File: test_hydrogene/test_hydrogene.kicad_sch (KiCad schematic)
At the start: 7 parts, among them U3 STM32G474RBTx

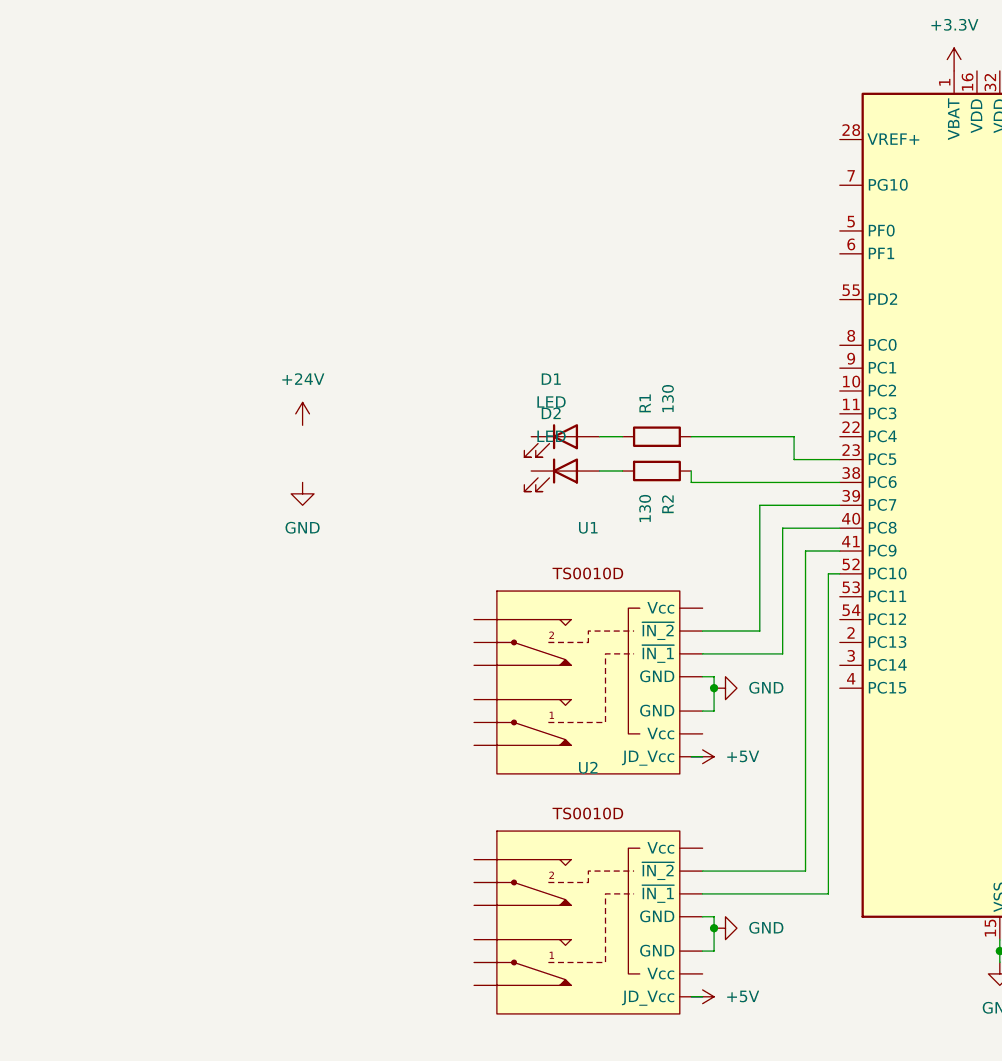
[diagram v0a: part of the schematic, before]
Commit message: Ajout des actuateurs
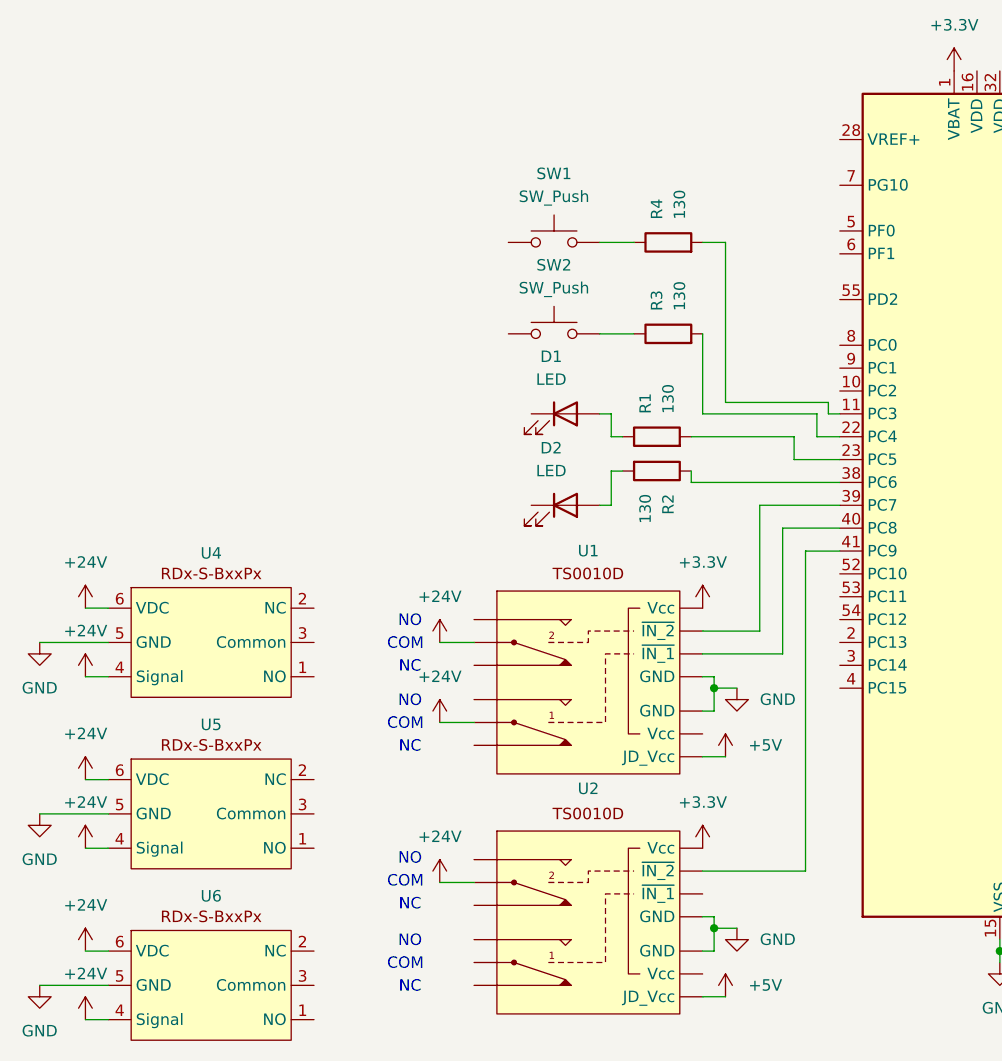
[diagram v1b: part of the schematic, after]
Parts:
- added R3, R4: 130, symbol Device:R
- added SW1, SW2: SW_Push, symbol Switch:SW_Push
- added U4, U5, U6: ~, symbol Actuator:RDx-S-BxxPx
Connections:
- net +24V: now also U1. (JD_Vcc), U2. (JD_Vcc), U4.4 (Signal), U4.6 (VDC), U5.4 (Signal), U5.6 (VDC), U6.4 (Signal), U6.6 (VDC)
- net +3.3V: now also U1. (JD_Vcc), U2. (JD_Vcc)
- net GND: now also U4.5 (GND), U5.5 (GND), U6.5 (GND)
- net at U3.11 (PC3): now also R4.2
- net at U3.22 (PC4): now also R3.2
- net at U3.52 (PC10): no longer U2. (JD_Vcc)
- new net: R4.1, SW1.2
- new net: R3.1, SW2.2
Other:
- note added: "COM"
- note added: "NC"
- note added: "NO"
- moved on the sheet: D1, D2

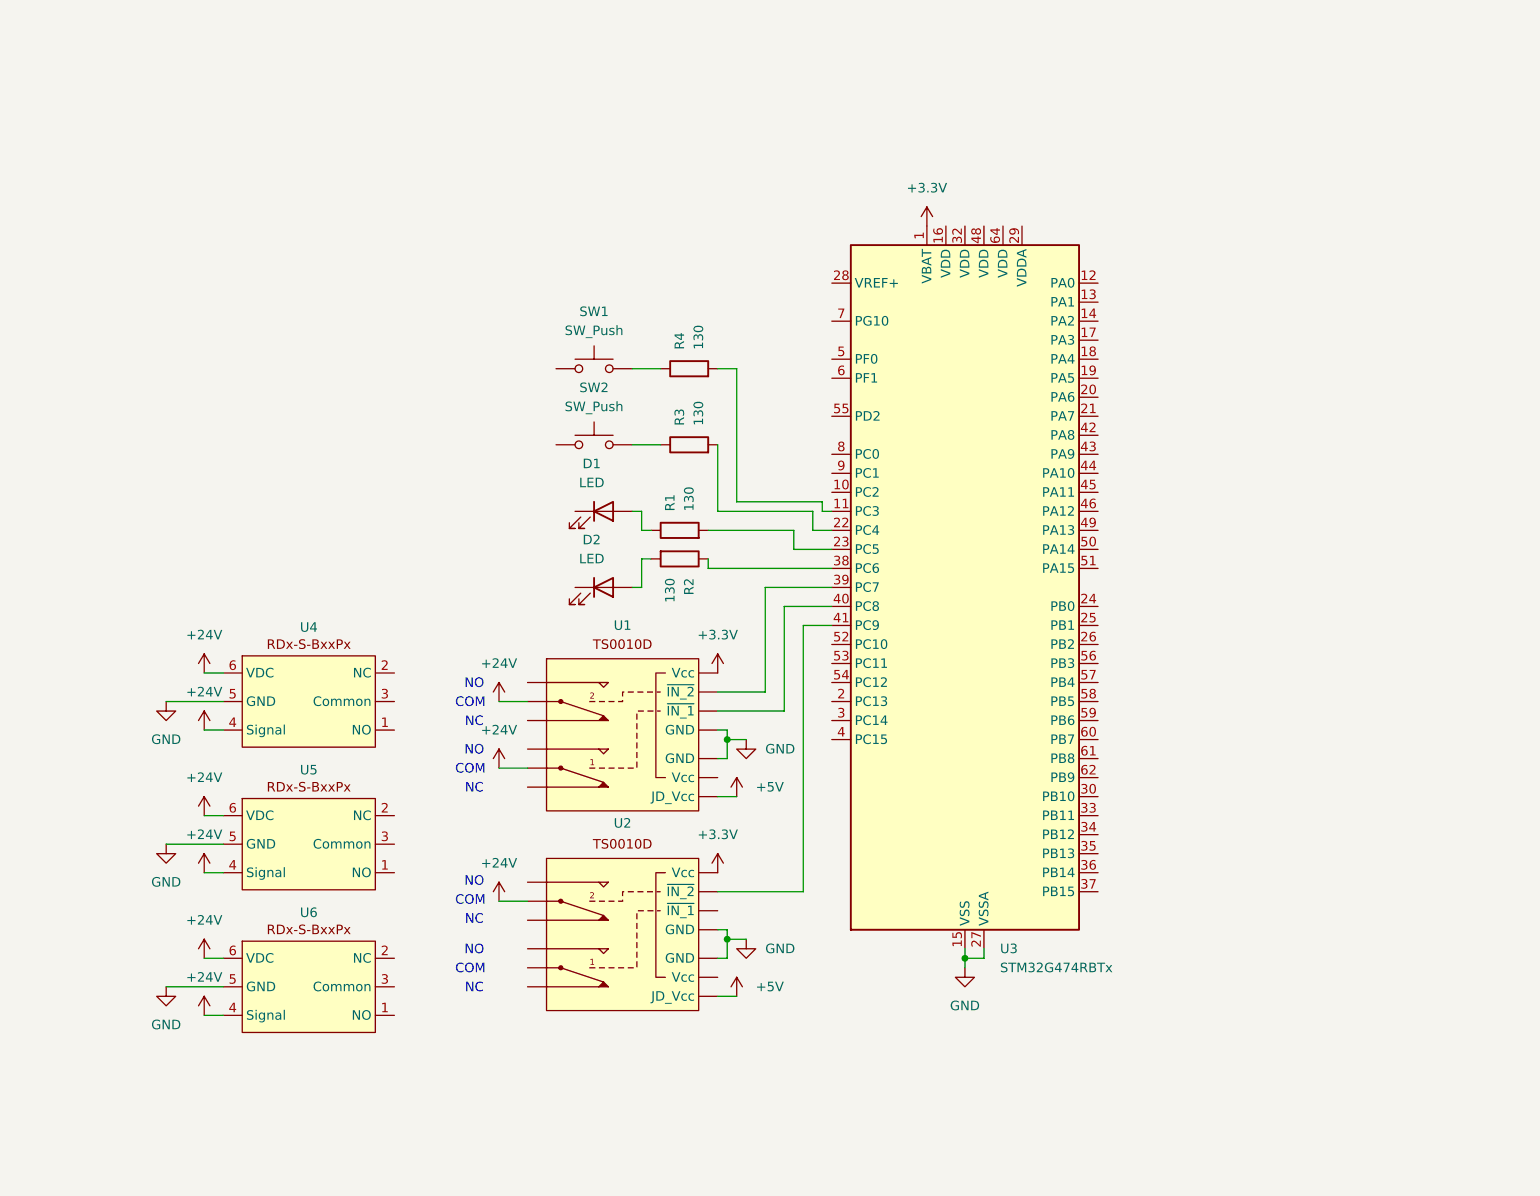
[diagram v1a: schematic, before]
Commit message: Connection des actuateurs
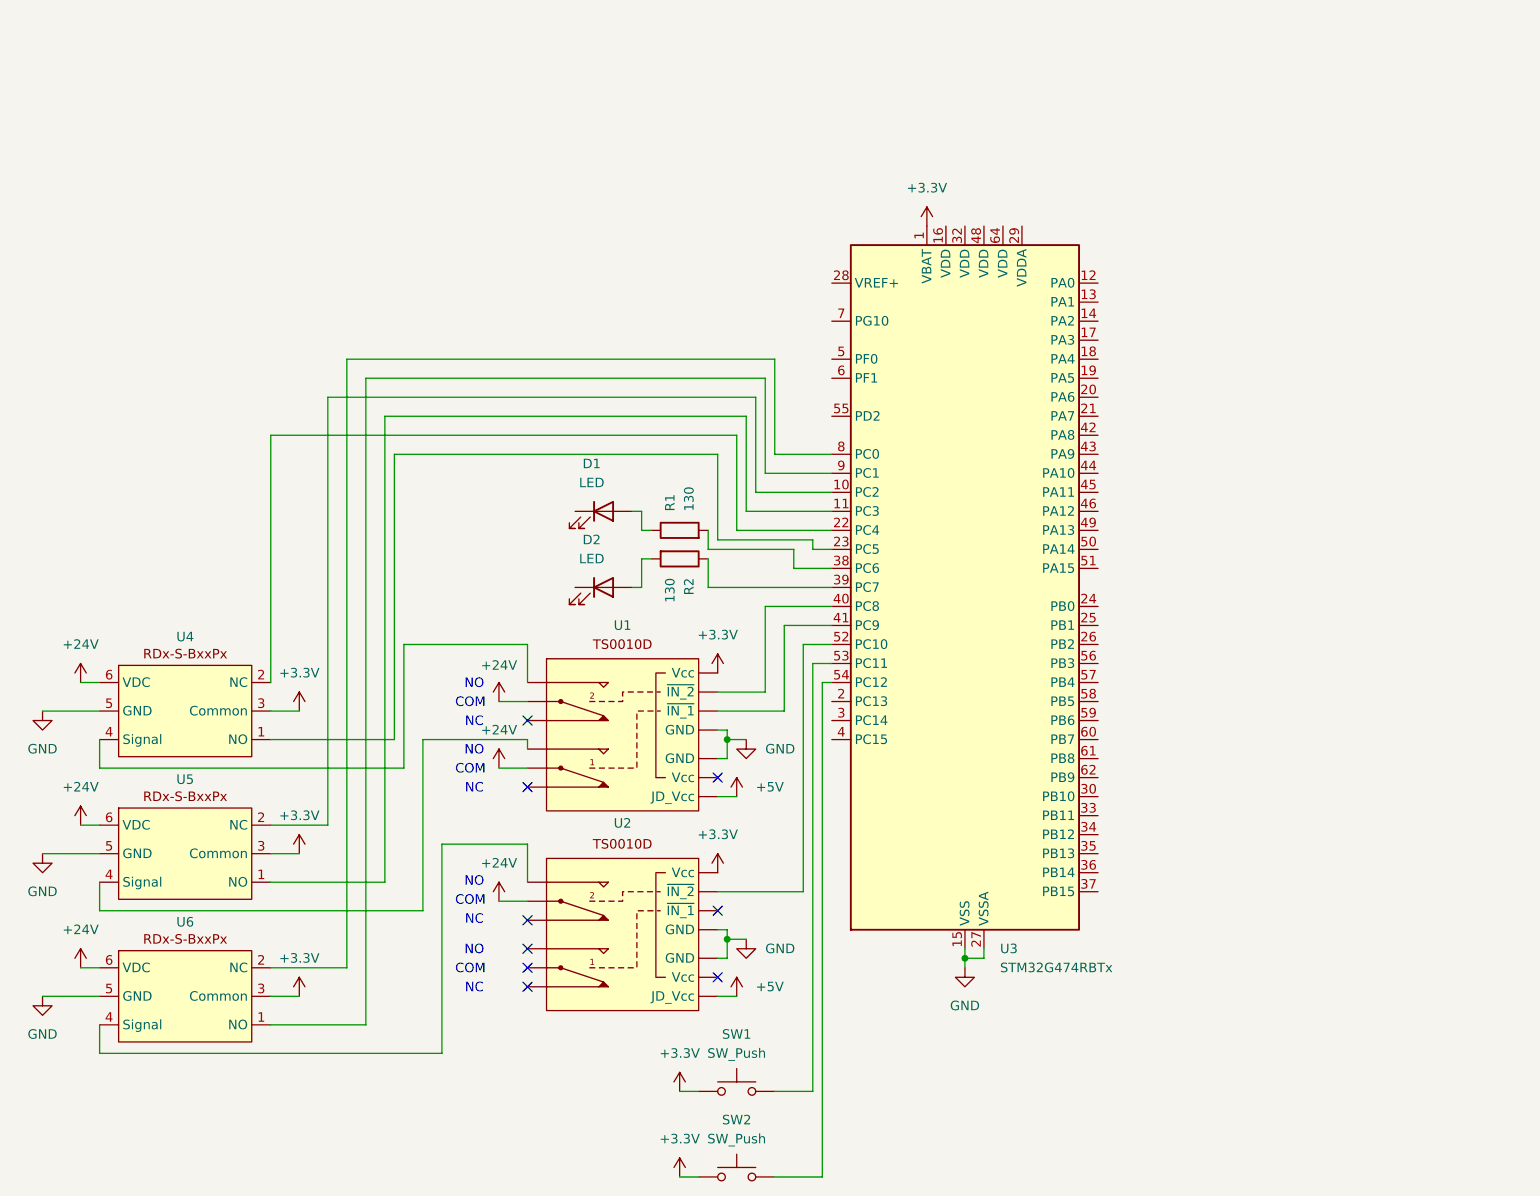
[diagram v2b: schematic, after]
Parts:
- removed R3, R4: 130, symbol Device:R
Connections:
- net +24V: no longer U4.4 (Signal), U5.4 (Signal), U6.4 (Signal)
- net +3.3V: now also SW1.1, SW2.1, U4.3 (Common), U5.3 (Common), U6.3 (Common)
- net at U5.1 (NO): now also U3.11 (PC3)
- net at U5.2 (NC): now also U3.10 (PC2)
- net at SW1.2: now also U3.53 (PC11)
- net at U3.39 (PC7): now also R2.1; no longer U1. (JD_Vcc)
- net at SW2.2: now also U3.54 (PC12)
- net at U6.1 (NO): now also U3.9 (PC1)
- net at U6.2 (NC): now also U3.8 (PC0)
- net at U3.22 (PC4): now also U4.2 (NC)
- net at U3.23 (PC5): now also U4.1 (NO); no longer R1.2
- net at U3.38 (PC6): now also R1.2; no longer R2.1
- net at U3.41 (PC9): now also U1. (JD_Vcc); no longer U2. (JD_Vcc)
- net at U3.52 (PC10): now also U2. (JD_Vcc)
- new net: U1. (JD_Vcc), U5.4 (Signal)
- new net: U1. (JD_Vcc), U4.4 (Signal)
- new net: U2. (JD_Vcc), U6.4 (Signal)
- no-connect marks 0 -> 9
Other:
- moved on the sheet: SW1, SW2, U4, U5, U6

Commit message: Simplifié le schéma
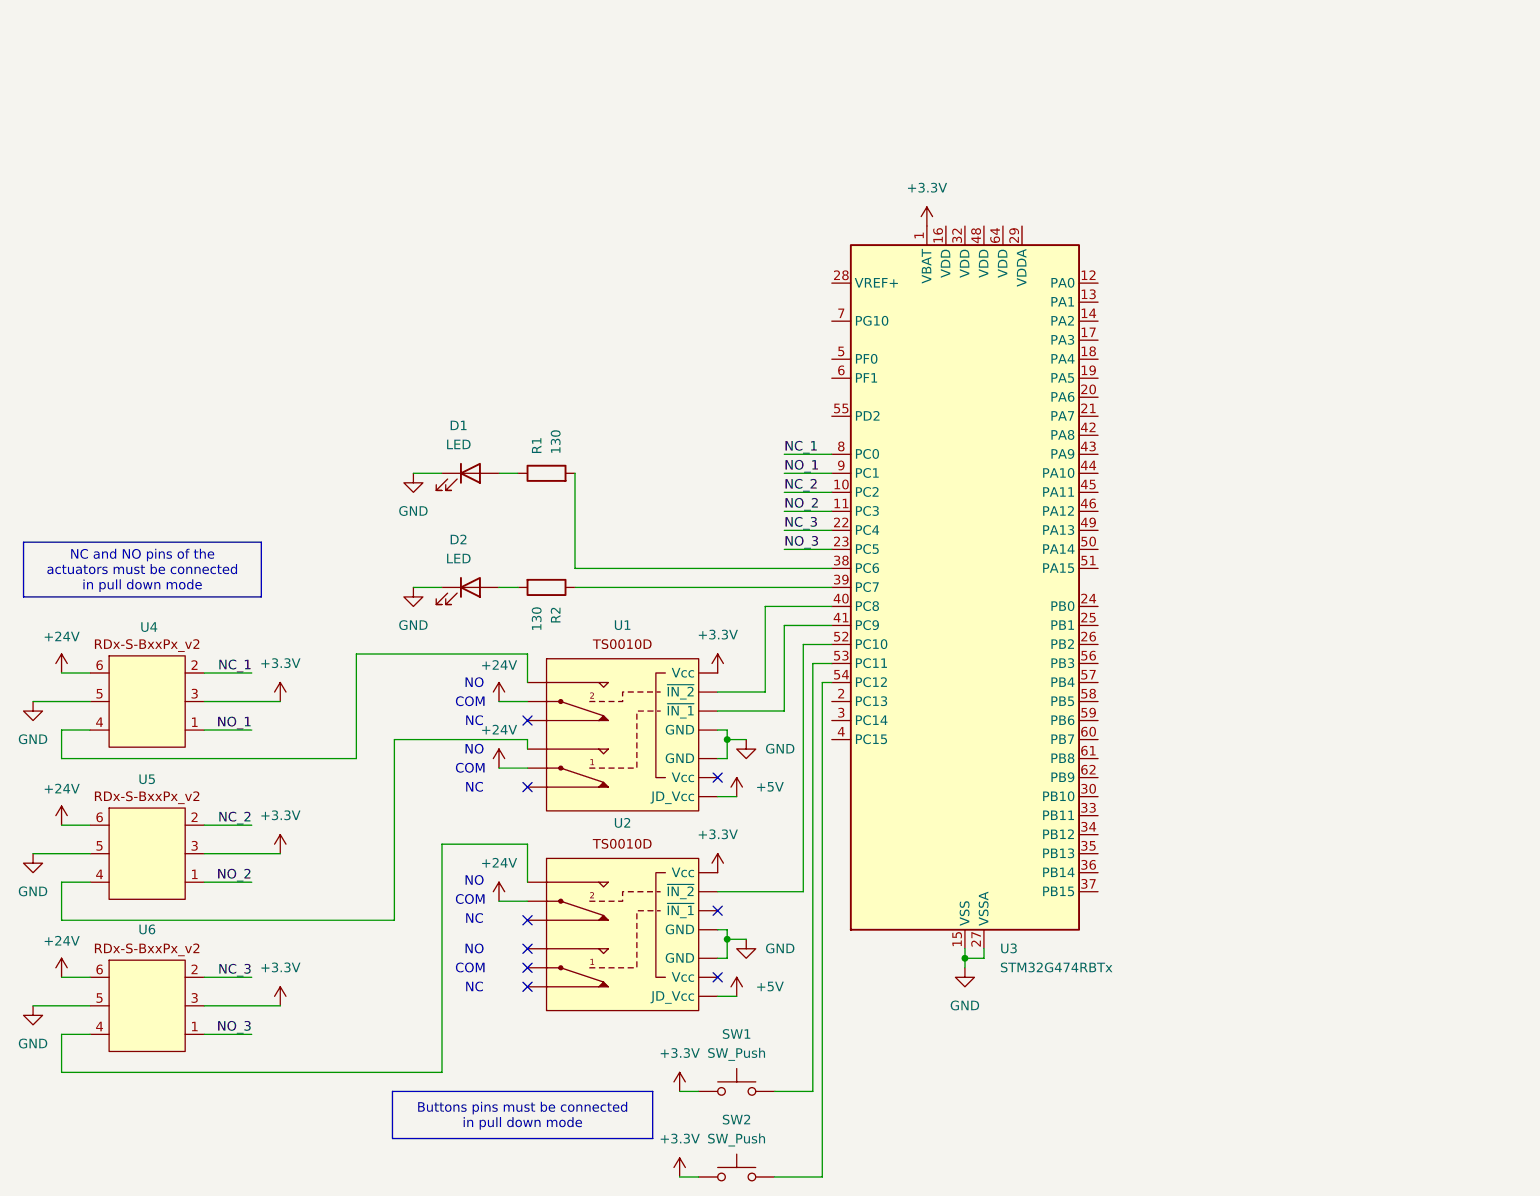
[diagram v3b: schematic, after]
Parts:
- removed U4, U5, U6: ~, symbol Actuator:RDx-S-BxxPx
- added U4, U5, U6: ~, symbol Actuator:RDx-S-BxxPx_v2
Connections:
- net +24V: now also U4.6, U5.6, U6.6
- net +3.3V: now also U4.3, U5.3, U6.3
- net GND: now also D1.1 (K), D2.1 (K), U4.5, U5.5, U6.5
- net NO_2: now reaches U3.11 (PC3)
- net NO_2: now also U5.1
- net NC_2: now reaches U3.10 (PC2)
- net NC_2: now also U5.2
- net NO_1: now reaches U3.9 (PC1)
- net NO_1: now also U4.1
- net NC_1: now reaches U3.8 (PC0)
- net NC_1: now also U4.2
- net NC_3: now reaches U3.22 (PC4)
- net NC_3: now also U6.2
- net NO_3: now reaches U3.23 (PC5)
- net NO_3: now also U6.1
- new net: U1. (JD_Vcc), U4.4
- new net: U1. (JD_Vcc), U5.4
- new net: U2. (JD_Vcc), U6.4
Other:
- company: (none) -> Exocet Polytechnique Montréal
- title: (none) -> Test Hydrogène
- moved on the sheet: D1, D2, R1, R2

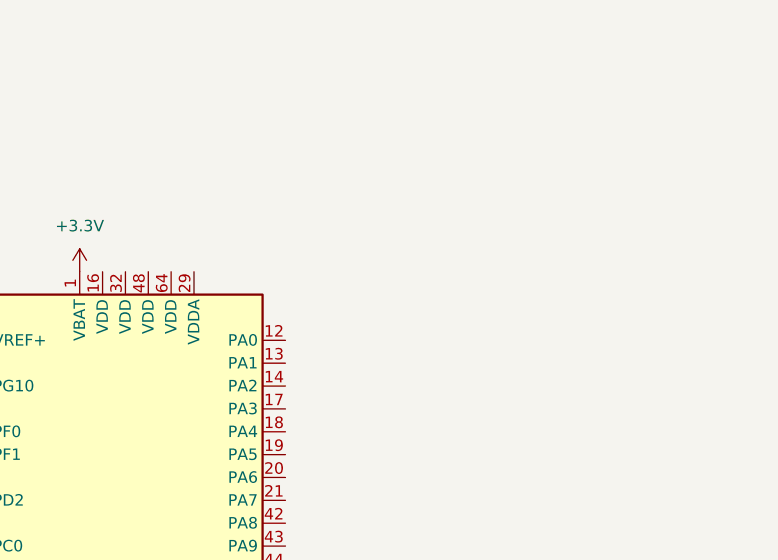
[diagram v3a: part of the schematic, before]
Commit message: Ajout du manomètre et diviseur de tension pour ADC
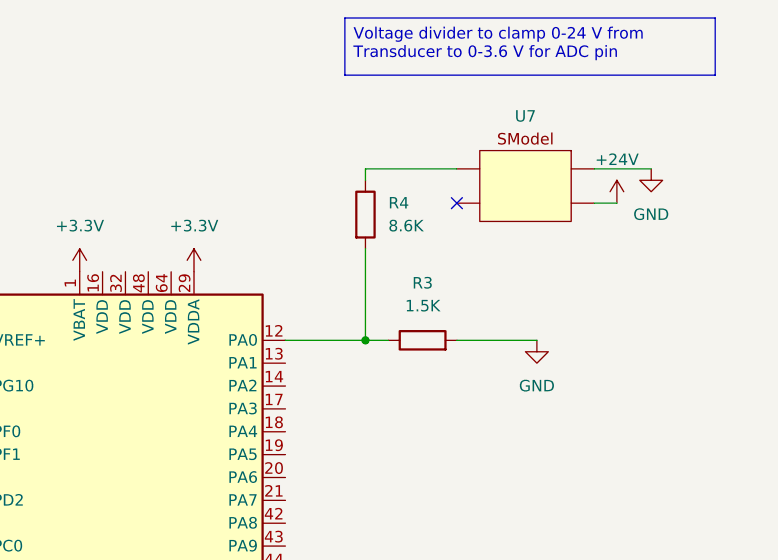
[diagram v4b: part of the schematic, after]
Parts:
- added R3: 1.5K, symbol Device:R
- added R4: 8.6K, symbol Device:R
- added U7: ~, symbol Transducer:SModel
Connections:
- net +24V: now also U7.
- net +3.3V: now also U3.29 (VDDA)
- net GND: now also R3.2, U7.
- net at U3.12 (PA0): now also R3.1, R4.2
- new net: R4.1, U7.
- no-connect marks 9 -> 10
